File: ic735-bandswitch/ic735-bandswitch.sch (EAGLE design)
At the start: 26 parts, among them IC2 ARDUINO_PRO_MICRO

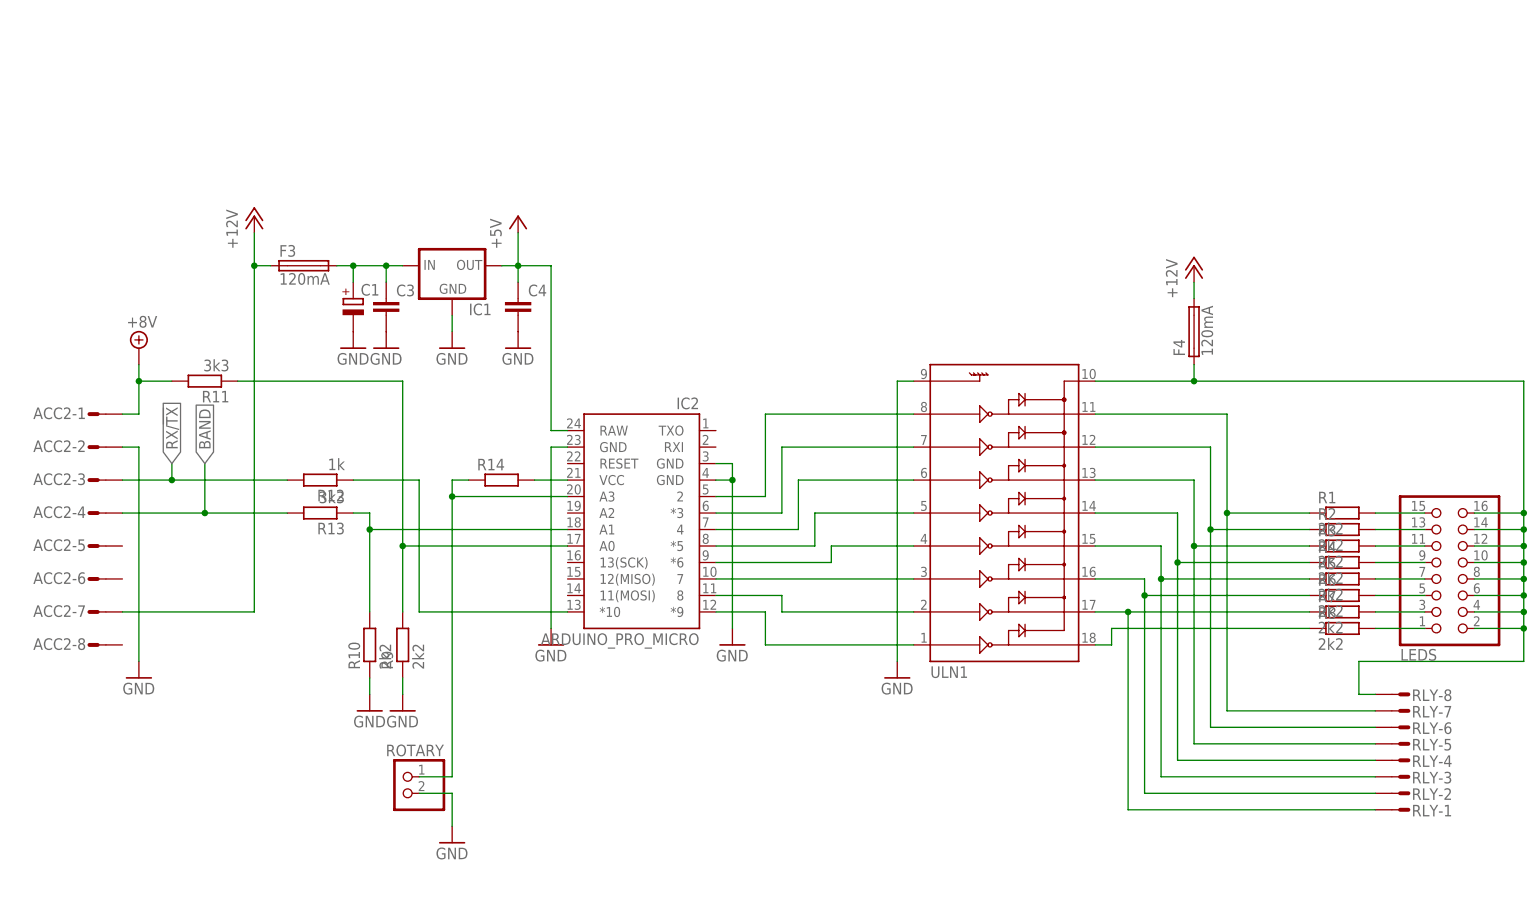
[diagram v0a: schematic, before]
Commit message: Add rotary switch and pdf
Add rotary switch for better understanding.
Add PDF files.
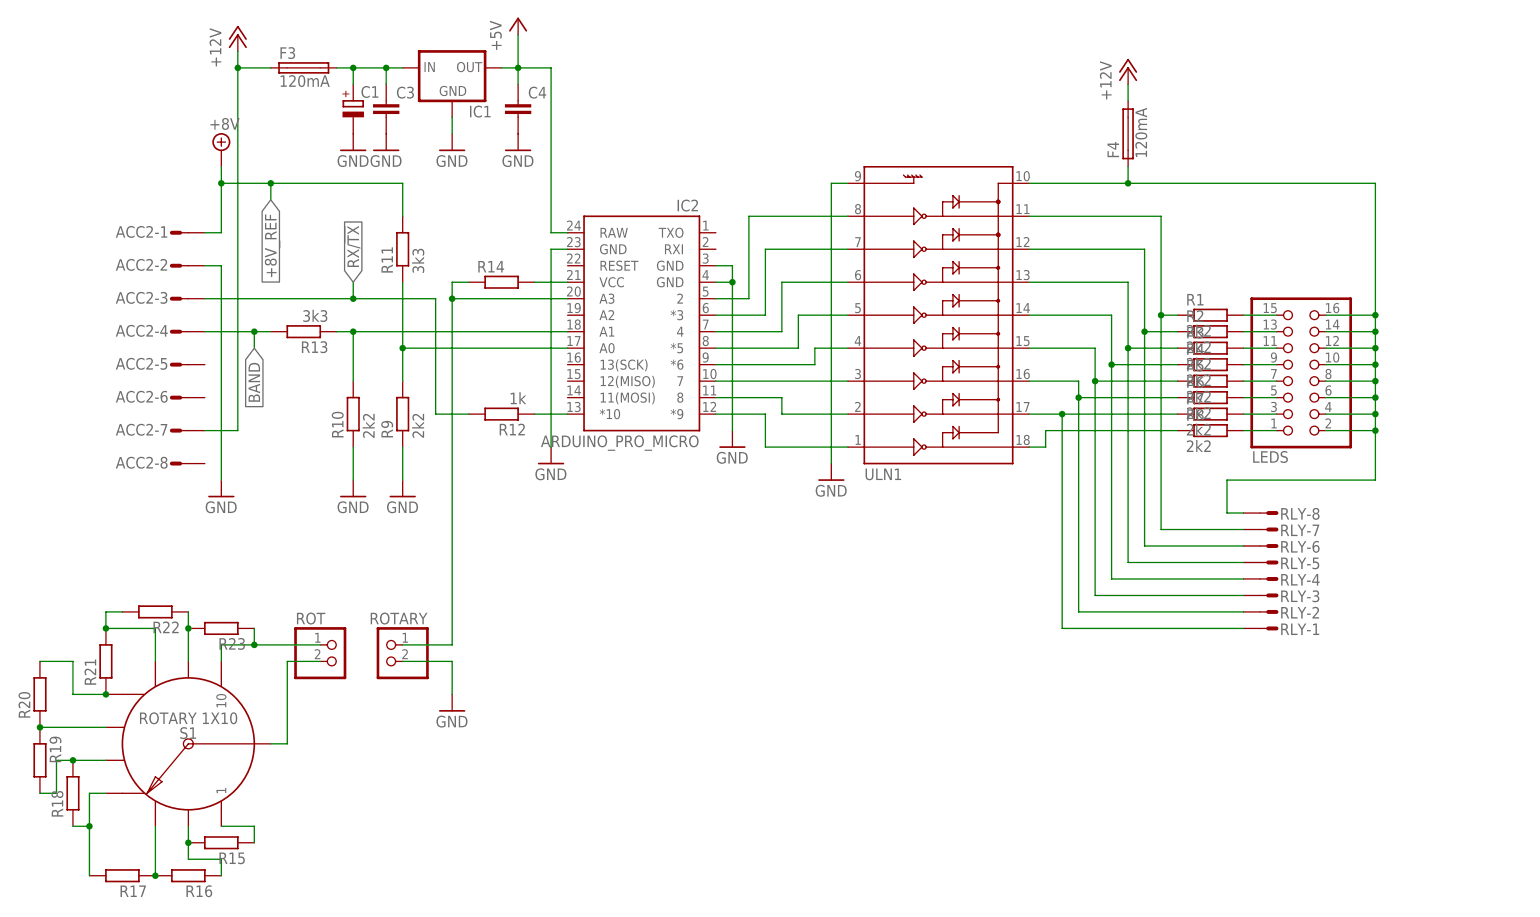
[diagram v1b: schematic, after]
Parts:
- added R15, R16, R17, R18, R19, R20, R21, R22, R23: (no value), rcl:R-EU_R0603
- added ROT: (no value), pinhead:PINHD-1X2
- added S1: ROTARY 1X10, SparkFun-Switches:SWITCH_ROTARY_1X10-PTH
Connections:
- net +8V renamed +8V_REF
- new net N$32: R15.1, S1.1
- new net N$33: R15.2, R16.1, S1.2
- new net N$34: R23.1, ROT.1, S1.10
- new net N$35: R16.2, R17.1, S1.3
- new net N$36: R19.1, R20.1, S1.6
- new net N$37: R17.2, R18.1, S1.4
- new net N$38: R18.2, R19.2, S1.5
- new net N$39: ROT.2, S1.COMMON
- new net N$40: R20.2, R21.1, S1.7
- new net N$41: R21.2, R22.2, S1.8
- new net N$42: R22.1, R23.2, S1.9
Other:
- moved on the sheet: ACC2-1, ACC2-2, ACC2-3, ACC2-4, ACC2-5, ACC2-6, ACC2-7, ACC2-8, C1, C3, C4, F3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
